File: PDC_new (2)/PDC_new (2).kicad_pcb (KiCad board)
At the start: 4 copper layers, 143 x 129 mm, 91 parts, among them J1 Conn_01x02_Pin, J10 Conn_01x02_Pin, J11 XT90PW(2+2)-M.G.Y, J12 Conn_01x02_Pin, J13 XT90PW-F, J2 Conn_01x02_Pin, J3 Conn_01x02_Pin, J4 Conn_01x02_Pin, J5 Conn_01x02_Pin, J6 Conn_01x02_Pin, J7 Conn_01x02_Pin, J8 Conn_01x02_Pin, J9 Conn_01x02_Pin, Q1 BSS123, Q2 IRF540NSTRLPBF, U1 TPSI3050QDWZRQ1, U10 LM393LVDR, U11 IPB017N10N5ATMA1, U12 IPB017N10N5ATMA1, U14 IPB017N10N5ATMA1, U2 TPSI3050QDWZRQ1, U3 TPSI3050QDWZRQ1, U4 74HC74, U5 URB4805LD-60WR3, U6 IPB017N10N5ATMA1, U7 TLC555CDR, U8 SN74HC08D, U9 SN74HC14DR

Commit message: Update PDC_new (2) PCB layout
Re-save of the board with updated placement and routing.

Co-Authored-By: Claude Sonnet 5.5 <noreply@anthropic.com>
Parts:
- removed C14: 470nF, Capacitor_SMD:C_1206_3216Metric
- removed C15: 470nF, Capacitor_SMD:C_0805_2012Metric
- removed C8: 1µF, Capacitor_SMD:C_0805_2012Metric
- removed D6: LED, LED_SMD:LED_0805_2012Metric
- removed F2, F3: 3568-15, Fuse:Fuseholder_Blade_Mini_Keystone_3568
- removed Q1: BSS123, Package_TO_SOT_SMD:SOT-23
- removed R19: 20k, Resistor_SMD:R_0805_2012Metric
- removed R2: 1k, Resistor_THT:R_Axial_Power_L25.0mm_W9.0mm_P30.48mm
- removed R30: 22k, Resistor_SMD:R_1206_3216Metric
- removed R7: 10, Resistor_SMD:R_0805_2012Metric
- removed R8: 10k, Resistor_SMD:R_0805_2012Metric
- removed U3: TPSI3050QDWZRQ1, ul_TPSI3050QDWZRQ1:DWZ0008A-MFG
- added D4: LED, LED_SMD:LED_0805_2012Metric, F.Cu at (333.4, 252.0)
- added R5: 1k, Resistor_SMD:R_0805_2012Metric, F.Cu at (328.6, 251.5)
- C12: value 2.2µF -> 4.3µF; footprint Capacitor_SMD:C_0805_2012Metric -> Capacitor_SMD:C_1206_3216Metric
- C13: value 2.2 µF -> 4.3 µF
- C5, C6: value C -> 100uF
- moved J1 137.6 mm to (367.5, 157.8), turned to -90 degrees
- moved J10 134.2 mm to (344.2, 144.7), turned to 0 degrees
- moved J9 124.0 mm to (326.6, 144.7), turned to 0 degrees
- moved J6 122.0 mm to (274.0, 144.7), turned to 0 degrees
- moved J2 119.4 mm to (367.5, 175.3), turned to -90 degrees
- moved J8 118.2 mm to (309.1, 144.7), turned to 0 degrees
- moved J7 117.6 mm to (291.6, 144.7), turned to 0 degrees
- moved J12 109.9 mm to (258.1, 158.5), turned to 90 degrees
- moved J3 104.0 mm to (367.5, 192.8), turned to -90 degrees
- moved RV1 102.4 mm to (321.6, 159.0), turned to 0 degrees
- moved F4 102.0 mm to (318.5, 178.5), turned to -90 degrees
- moved D1 94.0 mm to (290.5, 180.4)
- moved D3 94.0 mm to (290.5, 185.0)
- moved J4 92.8 mm to (367.5, 210.4), turned to -90 degrees
- moved J5 87.4 mm to (367.5, 227.9), turned to -90 degrees
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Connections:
- net /POR_N renamed /reset_N
- net /POR_RC renamed /reset_rc
- R1 pad 1: /PRE_FUSE -> /BATT+
- U9 pad 10: /EN_BLEED -> unconnected-(U9-5Y-Pad10)
- U9 pad 11: /RUN_OK -> unconnected-(U9-5A-Pad11)
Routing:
- net /BUS+: track 0.00 -> 565.3 mm, vias 33 -> 6
- net /BATT+: track 0.00 -> 251.0 mm, vias 8 -> 1
- net /RUN_N: track 135.3 -> 16.2 mm
- net /EN_BLEED: track 90.8 -> 0.00 mm
- net /FAULT_N: track 92.9 -> 25.1 mm, vias 0 -> 3
- net /BUCK_CTRL: track 15.8 -> 69.3 mm
- net Net-(J12-Pin_1): track 19.0 -> 70.3 mm
- net /DONE_N: track 43.0 -> 2.80 mm, vias 0 -> 2
- net /BUCK_IN: track 86.9 -> 47.5 mm, vias 0 -> 2
- net /+5V: track 242.3 -> 204.6 mm, vias 2 -> 13
- net Net-(D6-K): track 36.9 -> 0.00 mm
- net /MSTR_ON: track 51.5 -> 23.2 mm
- net /PRE_FUSE: track 14.1 -> 0.00 mm
- net /PC_DONE: track 63.5 -> 50.1 mm, vias 0 -> 4
- net /BATT_IN: track 12.3 -> 24.9 mm
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- added copper zone on F.Cu, net GND
- removed copper zone on B.Cu, net /BATT+
- removed copper zone on In2.Cu, net /BUS+
- removed copper zone on In1.Cu, net GND
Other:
- board size 143 x 129 mm -> 156.5 x 145.5 mm
- copper layers 4 -> 2

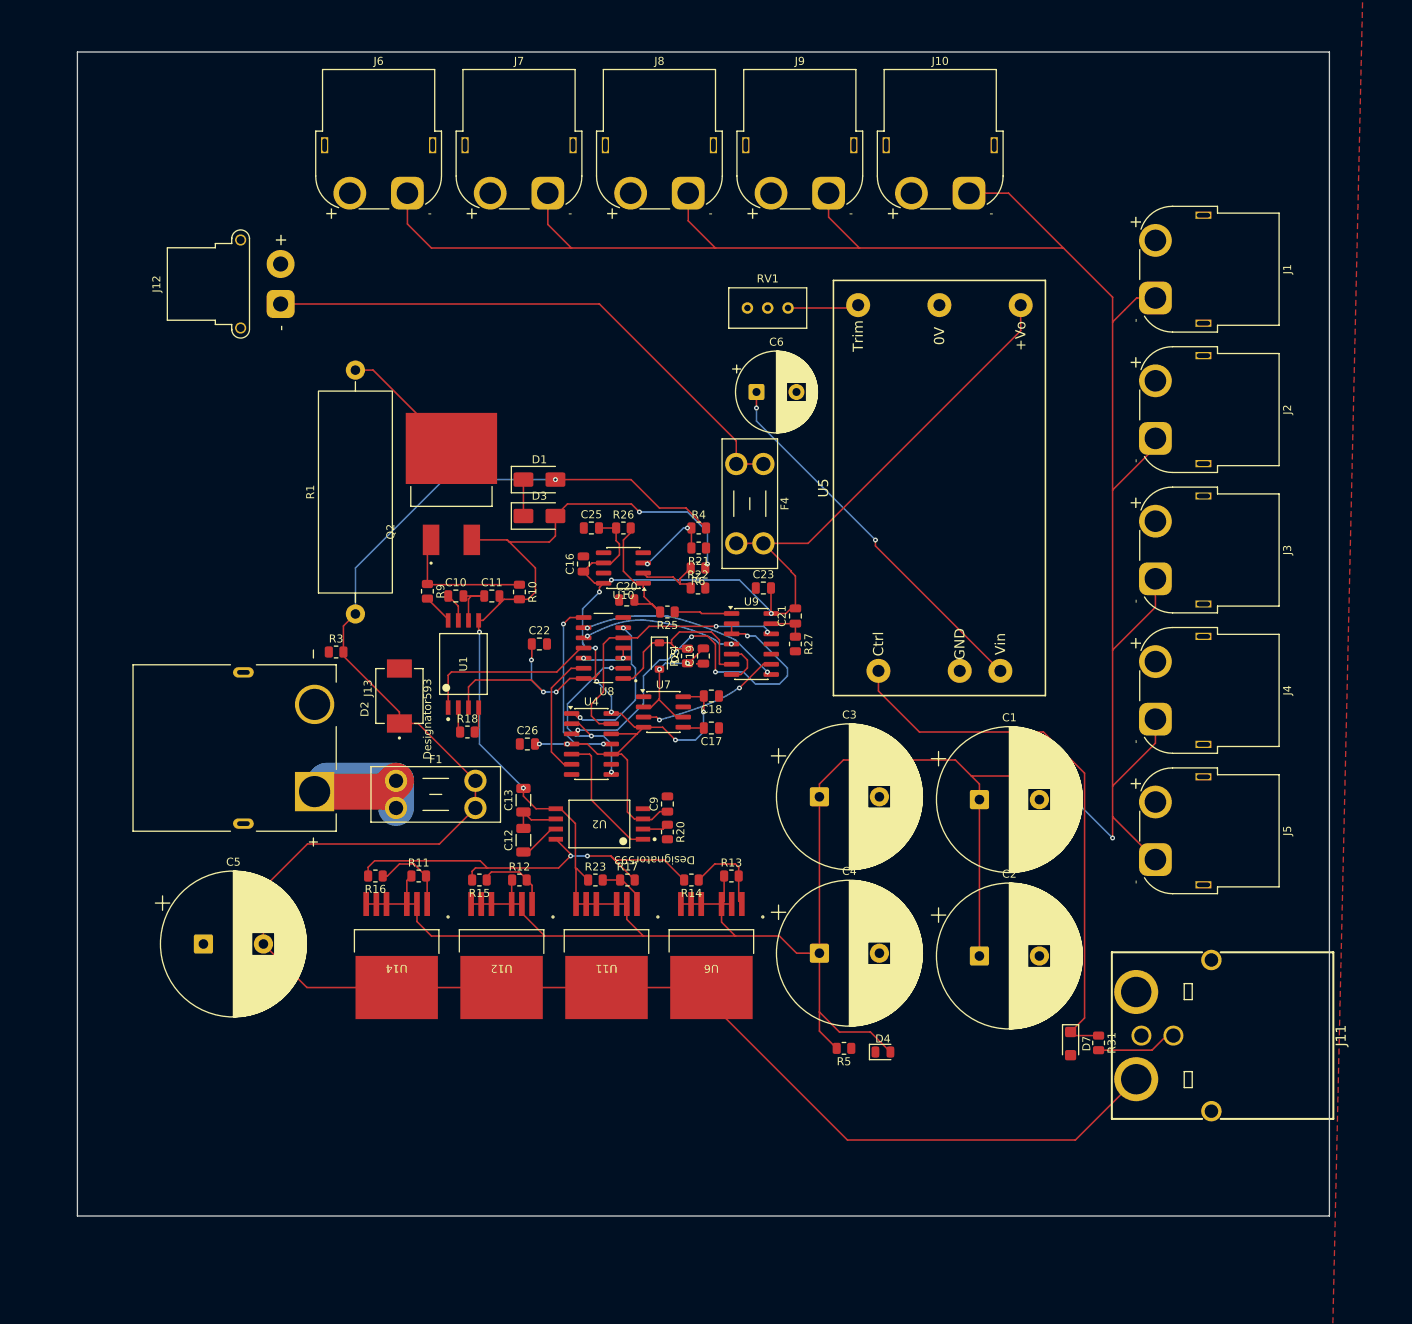
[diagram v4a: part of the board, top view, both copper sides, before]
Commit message: Change R5 to axial power THT footprint and update PCB layout
- Schematic: R5 (1k) footprint changed from R_0805 SMD hand-solder to
  Resistor_THT:R_Axial_Power_L25.0mm_W9.0mm_P30.48mm.
- PCB: board re-synced with updated footprints, re-routed tracks, added
  vias and copper zones.
- Project: default pad size updated to 1.95 x 0.6 mm SMD.

Co-Authored-By: Claude Opus 5.5 <noreply@anthropic.com>
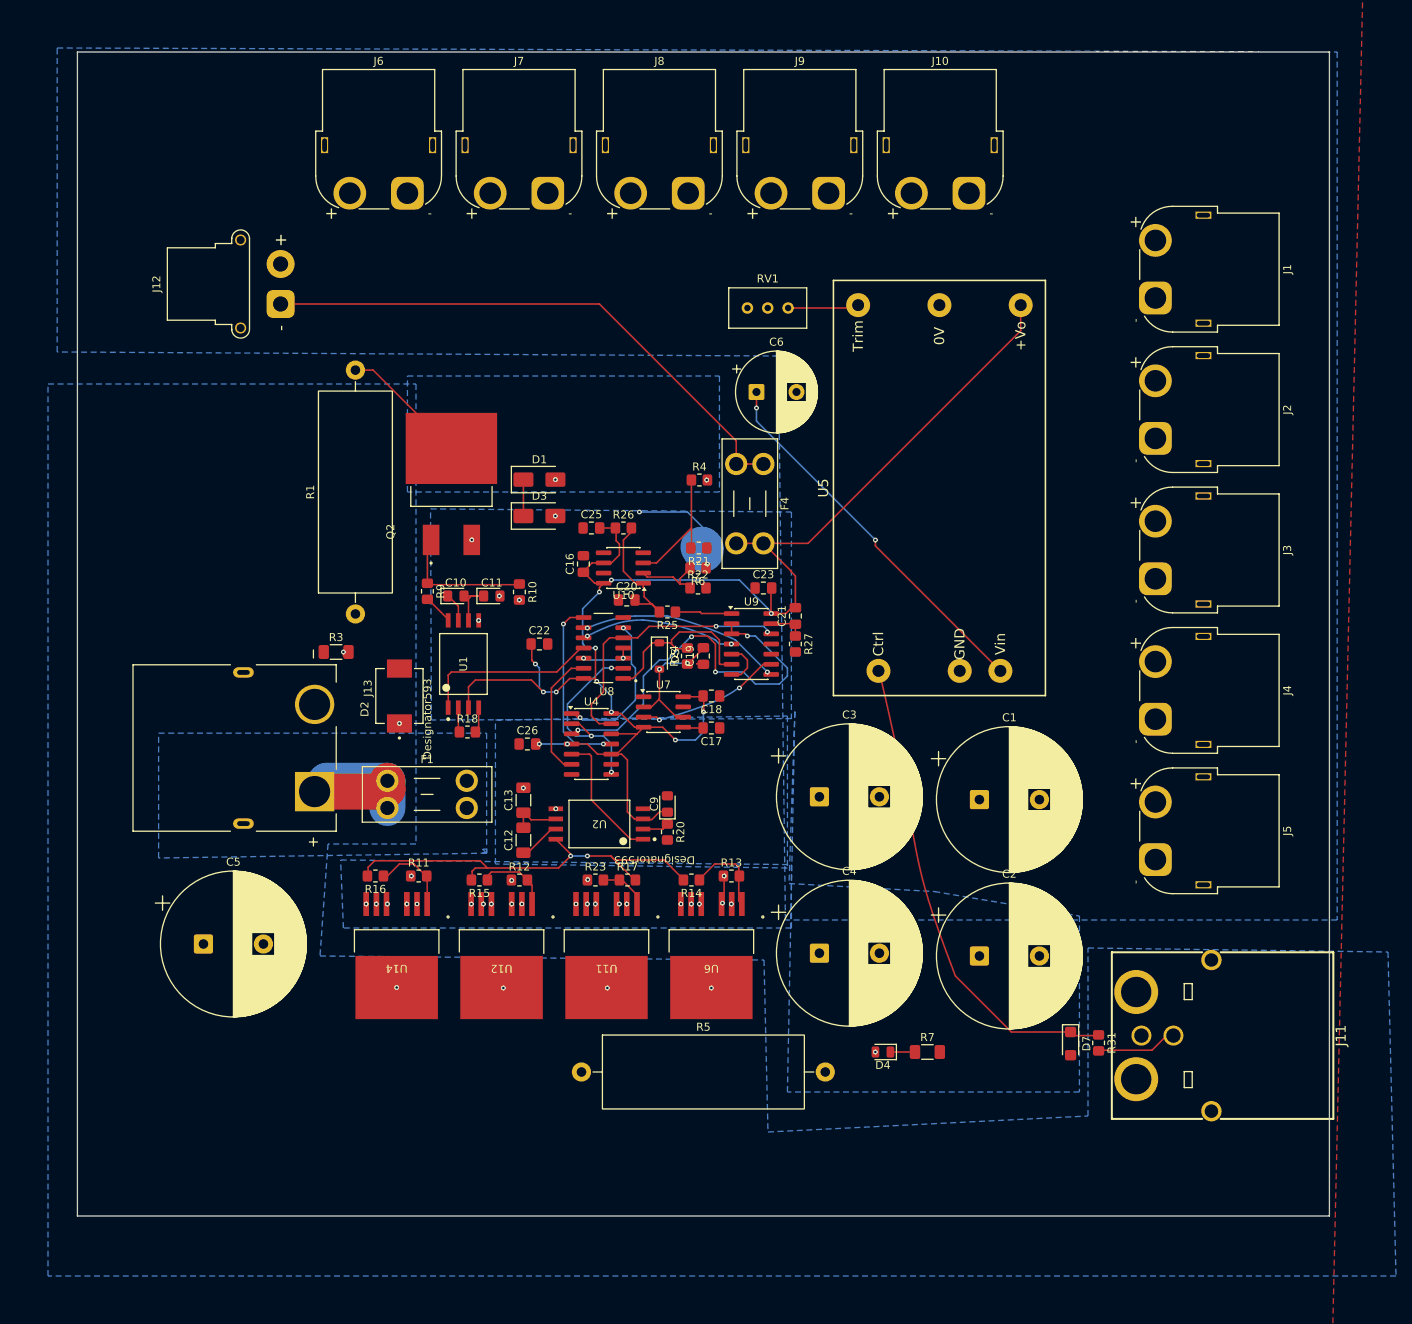
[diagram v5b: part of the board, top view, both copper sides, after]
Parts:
- added R7: 22k, Resistor_SMD:R_1206_3216Metric_Pad1.30x1.75mm_HandSolder, F.Cu at (339.0, 252.0)
- C10, C11, C9: footprint Capacitor_SMD:C_0805_2012Metric -> LED_SMD:LED_0805_2012Metric_Pad1.15x1.40mm_HandSolder
- C12, C13: footprint Capacitor_SMD:C_1206_3216Metric -> Capacitor_SMD:C_1206_3216Metric_Pad1.33x1.80mm_HandSolder
- C16, C17, C18, C19, C20, C21, C22, C23, C25, C26: footprint Capacitor_SMD:C_0805_2012Metric -> Capacitor_SMD:C_0805_2012Metric_Pad1.18x1.45mm_HandSolder
- R10, R11, R12, R13, R14, R15, R16, R17, R18, R20, R21, R22, R23, R24, R25, R26, R27, R31, R4, R6, R9: footprint Resistor_SMD:R_0805_2012Metric -> Resistor_SMD:R_0805_2012Metric_Pad1.20x1.40mm_HandSolder
- R3: footprint Resistor_SMD:R_0805_2012Metric -> Resistor_SMD:R_1206_3216Metric_Pad1.30x1.75mm_HandSolder
- R5: footprint Resistor_SMD:R_0805_2012Metric -> Resistor_THT:R_Axial_Power_L25.0mm_W9.0mm_P30.48mm
- moved R5 32.9 mm to (295.8, 254.5), turned to 0 degrees
- moved R4 6.00 mm to (310.5, 180.5)
- moved F1 1.08 mm to (271.5, 218.1)
- turned D4 to 180 degrees
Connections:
- D1 pad 1: /BUCK_OR -> /BUCK_IN
- D3 pad 1: /BUCK_OR -> /BUCK_IN
- D4 pad 1: GND -> Net-(D4-K)
- U9 pad 11: unconnected-(U9-5A-Pad11) -> GND
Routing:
- net /BUS+: track 565.3 -> 18.6 mm, vias 6 -> 34
- net /BATT+: track 251.0 -> 3.89 mm, vias 1 -> 8
- net /BUCK_CTRL: track 69.3 -> 21.0 mm
- net /BATT_SENSE: track 10.4 -> 17.0 mm, vias 2 -> 0
- net /BUCK_OR: track 4.55 -> 0.00 mm
- net /BUCK_IN: track 47.5 -> 52.0 mm
- net Net-(D4-K): track 0.00 -> 3.07 mm
- net /BATT_IN: track 24.9 -> 23.4 mm
- net /+5V: track 204.6 -> 203.6 mm
- added copper zone on B.Cu, net /BATT+
- added copper zone on B.Cu, net /BUS+

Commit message: Update PDC_new (2) PCB layout
Co-Authored-By: Claude Opus 5.5 <noreply@anthropic.com>
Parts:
- moved C19 2.50 mm to (308.5, 202.5)
- moved R24 2.00 mm to (311.0, 202.5), turned to -90 degrees
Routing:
- net /BUCK_IN: track 52.0 -> 86.3 mm, vias 2 -> 3
- net /DONE_N: track 2.80 -> 31.2 mm
- net /TIMEOUT: track 10.9 -> 32.9 mm
- net /PC_DONE: track 50.1 -> 30.5 mm, vias 4 -> 2
- net /MSTR_ON: track 23.2 -> 19.3 mm, vias 0 -> 2
- net /TIMER_RC: track 17.2 -> 20.5 mm, vias 2 -> 0
- net /+5V: track 203.6 -> 204.8 mm
- net GND: track 9.70 -> 8.98 mm, vias 0 -> 1
- net /BATT_IN: track 23.4 -> 22.8 mm
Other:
- outline, holes or cut-outs redrawn

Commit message: Update PDC_new (2) schematic, PCB layout and project settings
Co-Authored-By: Claude Opus 5.5 <noreply@anthropic.com>
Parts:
- added J14: Conn_01x02_Pin, Connector_AMASS:AMASS_XT60PW-F_1x02_P7.20mm_Horizontal, F.Cu at (361.9, 144.4)
- added J15: Conn_01x02_Pin, Connector_AMASS:AMASS_XT60PW-F_1x02_P7.20mm_Horizontal, F.Cu at (256.1, 144.7)
- J13: value XT90PW-F -> Conn_01x02_Pin; footprint XT90PW-F:AMASS_XT90PW-F -> QS8_S_Connectors:QS8-S-M_Vertical_DirectCup
- R5: value 1k -> 10k
- moved J5 3.17 mm to (367.9, 231.1)
- moved J13 2.92 mm to (252.0, 211.5), turned to 90 degrees
- moved J3 2.83 mm to (368.4, 195.6)
- moved J2 2.83 mm to (368.4, 178.0)
- moved J4 2.83 mm to (368.4, 213.1)
- moved J1 2.71 mm to (368.9, 160.1)
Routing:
- net /BATT_IN: track 22.8 -> 4.81 mm
- net (no net): track 0.00 -> 8.62 mm
- net /BATT+: track 3.89 -> 1.26 mm, vias 8 -> 99
- net /MSTR_ON: track 19.3 -> 18.3 mm
- added copper zone on B.Cu, net /BATT_IN
- added copper zone on F.Cu, net /BATT_IN

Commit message: Update PDC_new (2) PCB layout
Co-Authored-By: Claude Opus 5.5 <noreply@anthropic.com>
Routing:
- net /TIMEOUT: track 32.9 -> 35.6 mm
- net /BATT+: track 1.26 -> 3.76 mm
- net /+5V: track 204.8 -> 202.5 mm
- net /FAULT_N: track 25.1 -> 27.1 mm
- net /reset_N: track 35.1 -> 36.2 mm, vias 2 -> 1
- net GND: track 8.98 -> 8.84 mm, vias 1 -> 0
- net /BUS+: track 18.2 -> 18.4 mm, vias 34 -> 43
